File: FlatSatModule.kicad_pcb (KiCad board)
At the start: 4 copper layers, 68.6 x 119.4 mm, 8 parts, among them J1 DB15_Female_HighDensity, J2 Micro_SD_Card_Det, J3 HEADER_15

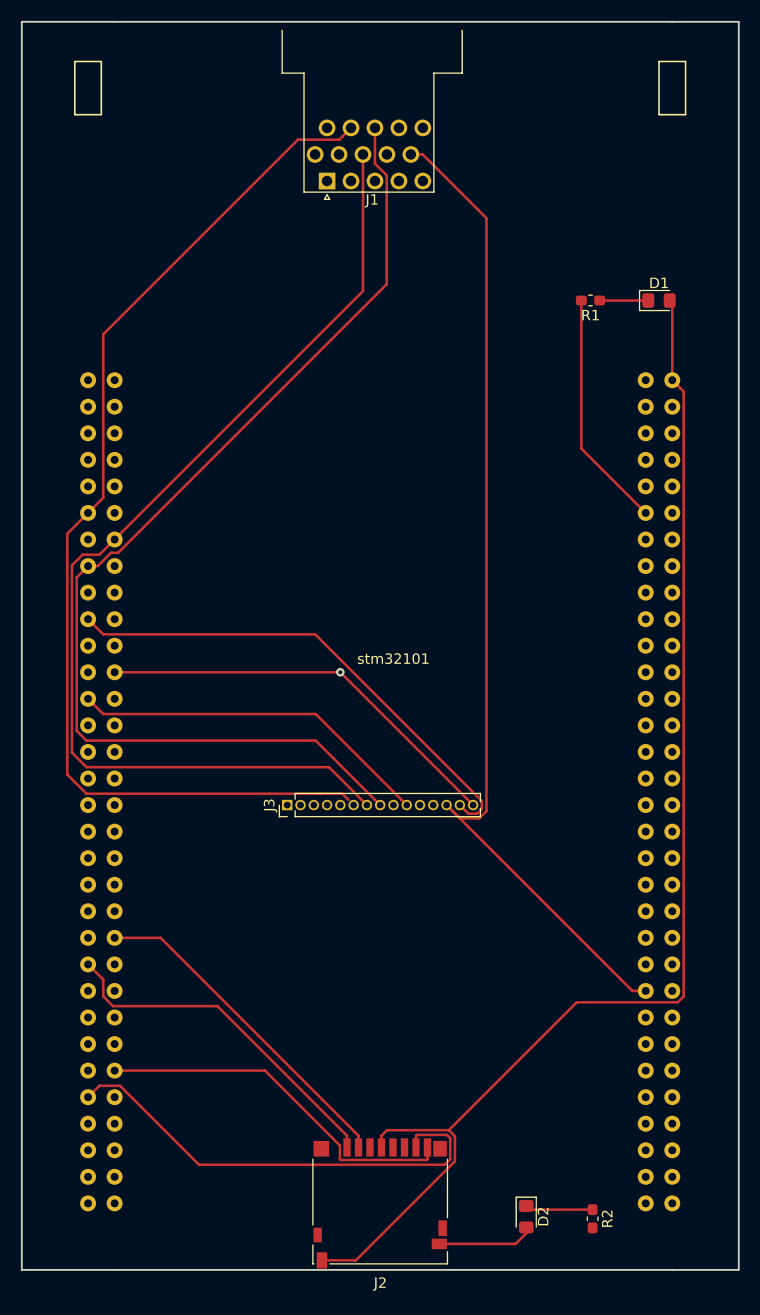
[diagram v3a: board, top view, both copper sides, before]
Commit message: add USARTs and gnd plane filling
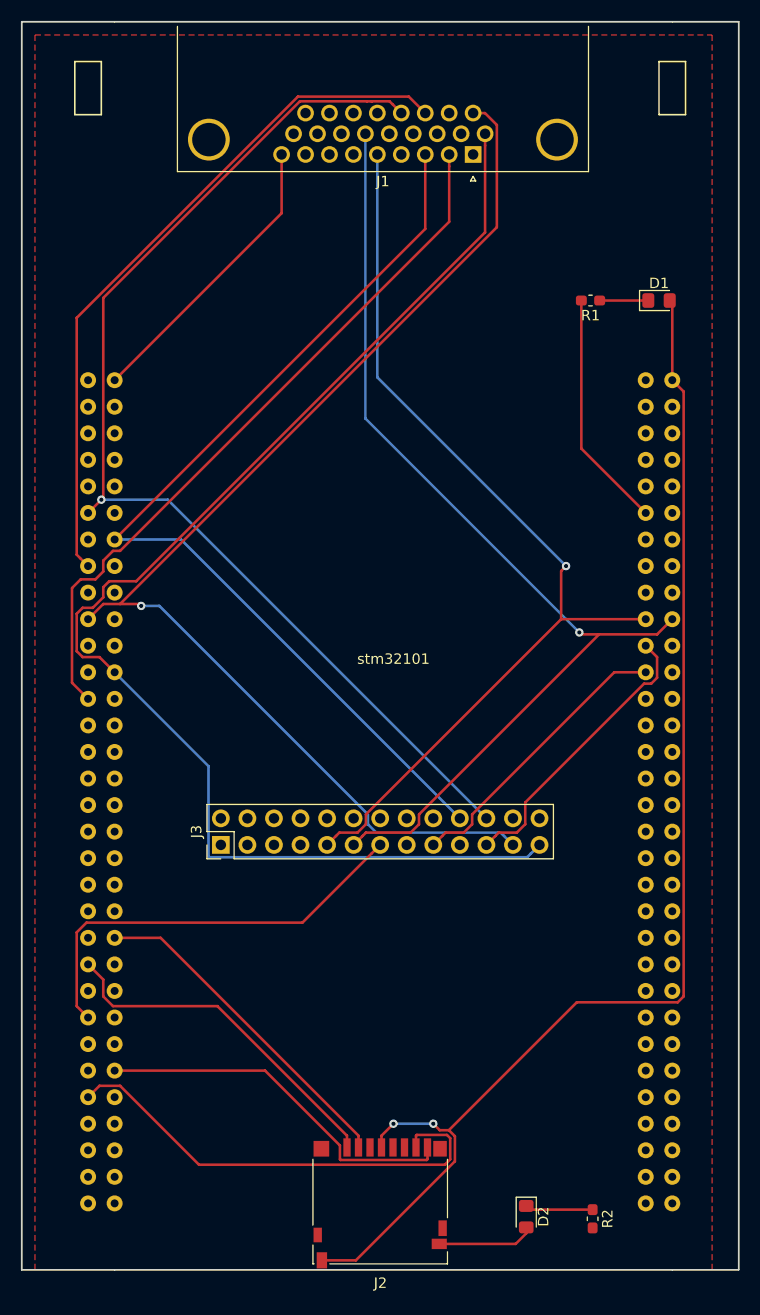
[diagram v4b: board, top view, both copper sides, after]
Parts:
- J1: value DB15_Female_HighDensity -> DB26_Male_HighDensity_MountingHoles; footprint Connector_Dsub:DSUB-15-HD_Female_Horizontal_P2.29x2.54mm_EdgePinOffset9.40mm -> Connector_Dsub:DSUB-26-HD_Male_Horizontal_P2.29x1.98mm_EdgePinOffset8.35mm_Housed_MountingHolesOffset10.89mm
- J3: value HEADER_15 -> HEADER_13x2; footprint Connector_PinHeader_1.27mm:PinHeader_1x15_P1.27mm_Vertical -> Connector_PinHeader_2.54mm:PinHeader_2x13_P2.54mm_Vertical
- moved J1 14.2 mm to (100.3, 52.1)
- moved J3 7.41 mm to (76.2, 118.1)
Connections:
- D1 pad 2: VCC -> /SD_DETA
- J1 pad 1: Net-(J1-Pad1) -> /I2C2_SDA
- J1 pad 10: /I2C2_SDA -> /I2C1_SDA
- J1 pad 11: Net-(J1-Pad11) -> /PA5
- J1 pad 12: /PE6 -> /PA7
- J1 pad 13: /PE2 -> /CAN1_RX
- J1 pad 14: /I2C2_SCL -> /PA9
- J1 pad 15: /I2C1_SCL -> /PA2
- J1 pad 2: Net-(J1-Pad2) -> /PB4
- J1 pad 3: /PA7 -> /PE5
- J1 pad 4: /PA5 -> /CAN1_TX
- J1 pad 5: /I2C1_SDA -> /PA3
- J1 pad 8: /PE5 -> Net-(J1-Pad8)
- J1 pad 9: /PB4 -> VCC
- J2 pad 10: VCC -> /SD_DETA
- J2 pad 4: VCC -> /SD_DETA
- J3 pad 10: /PB4 -> Net-(J3-Pad10)
- J3 pad 11: /PA5 -> /PA2
- J3 pad 12: /I2C2_SDL -> Net-(J3-Pad12)
- J3 pad 13: /I2C2_SDA -> /CAN1_TX
- J3 pad 14: /I2C1_SCL -> /PA10
- J3 pad 15: /I2C1_SDA -> /CAN1_RX
- J3 pad 6: /PE6 -> Net-(J3-Pad6)
- J3 pad 7: /PE5 -> Net-(J3-Pad7)
- J3 pad 8: /PE2 -> Net-(J3-Pad8)
- J3 pad 9: /PA7 -> /PA3
- stm32101 pad 1: /VCC5 -> VCC
- stm32101 pad 2: /VCC5 -> VCC
- stm32101 pad 49: /PA12 -> /CAN1_TX
- stm32101 pad 50: /PA11 -> /CAN1_RX
- stm32101 pad 65: VCC -> /SD_DETA
- stm32101 pad 66: VCC -> /SD_DETA
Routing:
- net /SD_DETA: track 0.00 -> 123.0 mm, vias 0 -> 2
- net /PA10: track 0.00 -> 119.9 mm
- net /CAN1_RX: track 0.00 -> 114.4 mm
- net /CAN1_TX: track 0.00 -> 114.0 mm
- net /PA9: track 0.00 -> 104.1 mm
- net /PA2: track 0.00 -> 98.1 mm, vias 0 -> 1
- net VCC: track 122.5 -> 28.2 mm
- net /PA3: track 0.00 -> 92.1 mm, vias 0 -> 1
- net /I2C1_SDA: track 89.8 -> 125.7 mm, vias 1 -> 0
- net /PB4: track 99.5 -> 114.2 mm
- net /PE2: track 103.3 -> 115.4 mm
- net /I2C2_SDA: track 97.5 -> 86.8 mm
- net /PE5: track 100.0 -> 93.2 mm
- net /PE6: track 103.3 -> 107.7 mm, vias 0 -> 1
- net /I2C1_SCL: track 111.0 -> 114.8 mm, vias 0 -> 1
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- added copper zone on F.Cu, net GND

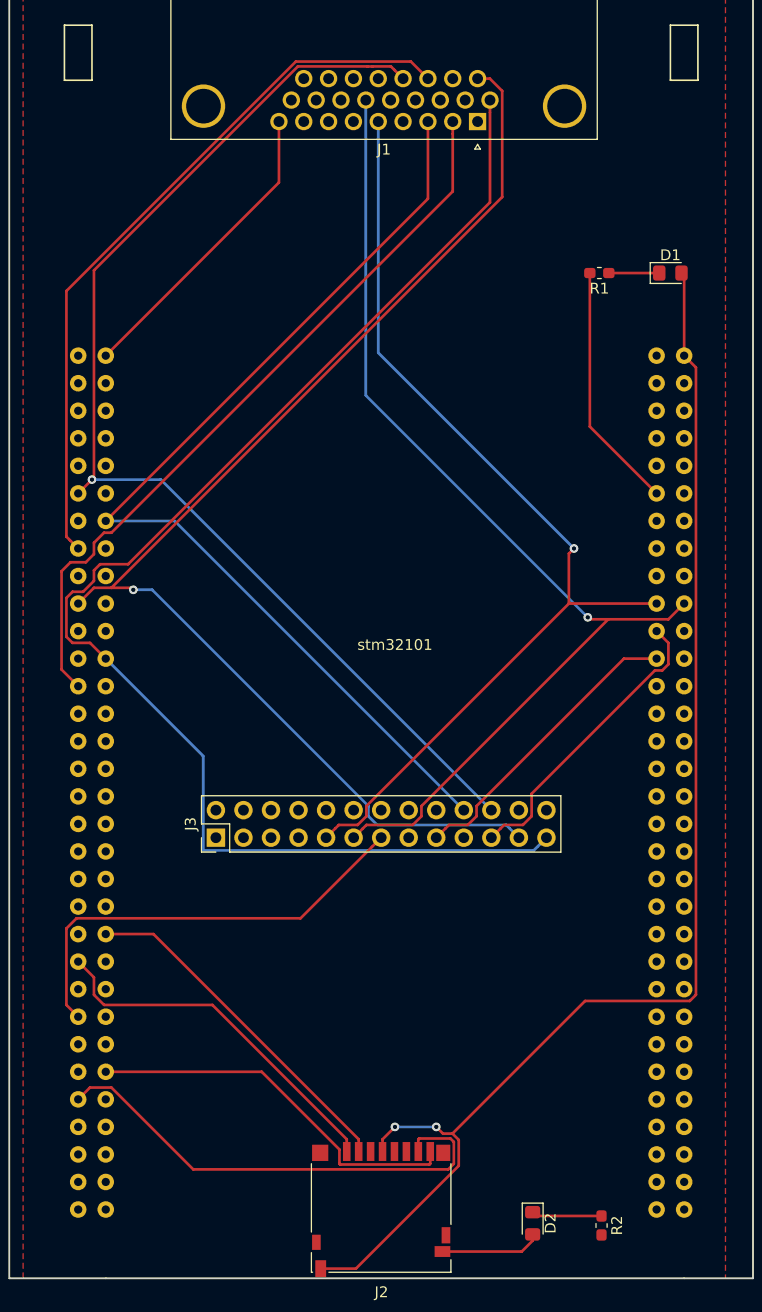
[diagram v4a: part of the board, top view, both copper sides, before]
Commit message: Add SS for SPI buses
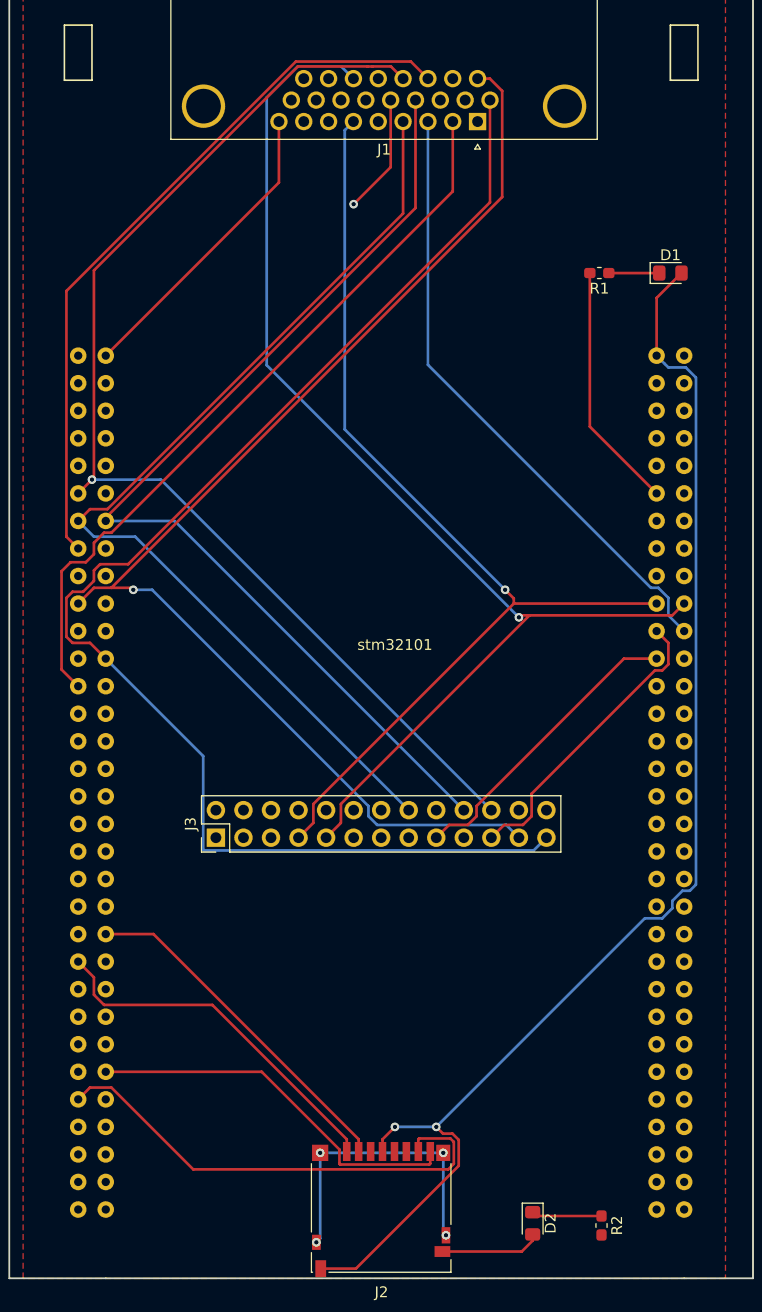
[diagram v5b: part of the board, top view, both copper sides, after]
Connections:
- J1 pad 13: /CAN1_RX -> /PE5
- J1 pad 14: /PA9 -> /CAN1_RX
- J1 pad 15: /PA2 -> /PA9
- J1 pad 24: Net-(J1-Pad24) -> /PA2
- J1 pad 3: /PE5 -> /PA4
- J1 pad 4: /CAN1_TX -> /PE4
- J1 pad 5: /PA3 -> /CAN1_TX
- J1 pad 6: Net-(J1-Pad6) -> /PA3
- J3 pad 11: /PA2 -> /CAN1_TX
- J3 pad 12: Net-(J3-Pad12) -> /PA10
- J3 pad 13: /CAN1_TX -> /CAN1_RX
- J3 pad 14: /PA10 -> /PA9
- J3 pad 15: /CAN1_RX -> /PA4
- J3 pad 16: /PA9 -> /PE4
- J3 pad 7: Net-(J3-Pad7) -> /PA3
- J3 pad 9: /PA3 -> /PA2
- stm32101 pad 1: VCC -> Net-(stm32101-Pad1)
- stm32101 pad 128: GND -> Net-(stm32101-Pad128)
- stm32101 pad 63: GND -> Net-(stm32101-Pad63)
- stm32101 pad 66: /SD_DETA -> Net-(stm32101-Pad66)
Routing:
- net /PA4: track 0.00 -> 99.2 mm
- net /PE4: track 0.00 -> 91.7 mm
- net Net-(J2-Pad11): track 0.00 -> 27.4 mm, vias 0 -> 4
- net /PA2: track 98.1 -> 111.3 mm
- net /CAN1_RX: track 114.4 -> 102.7 mm, vias 0 -> 1
- net GND: track 22.9 -> 31.2 mm
- net /PA3: track 92.1 -> 94.2 mm
- net /PE5: track 93.2 -> 95.1 mm
- net /CAN1_TX: track 114.0 -> 112.2 mm
- net /PA10: track 119.9 -> 121.2 mm
- net /SD_DETA: track 123.0 -> 121.9 mm
